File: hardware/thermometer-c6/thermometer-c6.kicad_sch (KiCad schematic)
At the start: 99 parts, among them J1 JST-PH-2 BAT, J2 MEAS_HDR, J3 USB-C, J4 EPD FPC24 0.5mm, J5 DEBUG, Q1 AO3401A, Q2 AO3401A, Q3 Si1308EDL, Q4 AO3401A, Q5 2N7002, Q6 AO3401A, SW1 RESET, SW2 BOOT, U1 ESP32-C6-MINI-1-N4, U2 RT9080-33GJ5, U3 USBLC6-2SC6, U4 MCP73831-2, U5 BMP581, U6 BMP585, Y1 32.768kHz FC-135

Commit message: Draw XUNPU FPC-05FB-24PH20 footprint, swap J4 off the Hirose stand-in
Land pattern transcribed from the XUNPU FPC-05FB-NPH20 manufacture
drawing and cross-checked against the EasyEDA/JLC C2856831 pattern
(exact match): 24 pads 0.3x1.2 @0.5mm, tabs 2.0x1.8 at +/-7.3/+1.625.
Cable enters from the pad-row side, actuator flips at the rear, pin 1
on the right with cable entry up (silk dot).

Co-Authored-By: Claude Fable 5 <noreply@anthropic.com>
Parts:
- J4: footprint Connector_FFC-FPC:Hirose_FH12-24S-0.5SH_1x24-1MP_P0.50mm_Horizontal -> local:XUNPU_FPC-05FB-24PH20
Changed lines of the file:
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@@
       )
     )
-    (property "Footprint" "Connector_FFC-FPC:Hirose_FH12-24S-0.5SH_1x24-1MP_P0.50mm_Horizontal"
+    (property "Footprint" "local:XUNPU_FPC-05FB-24PH20"
       (at 215.9 185.42 0)
       (effects

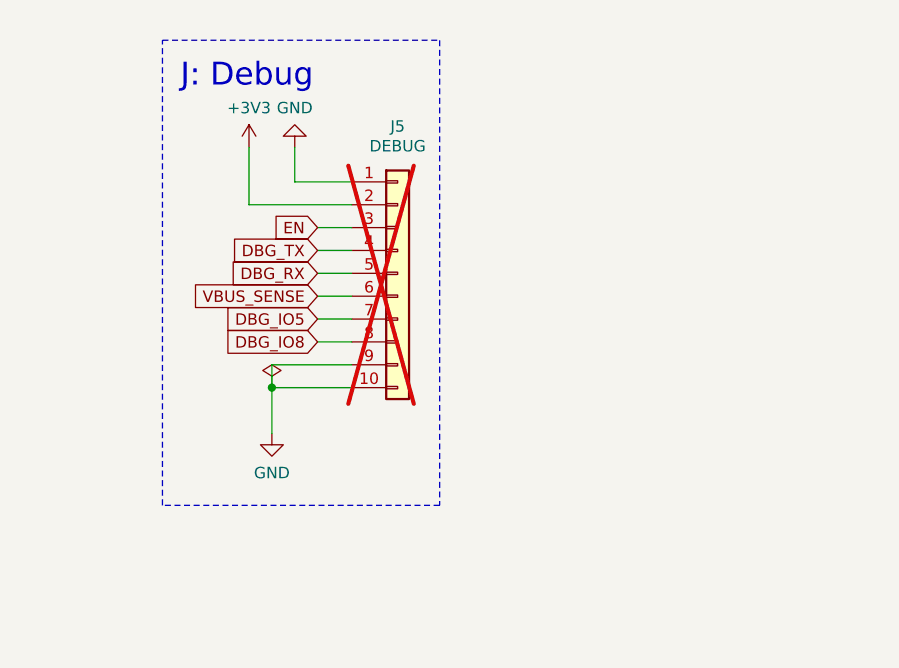
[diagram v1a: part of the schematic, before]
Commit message: Add scripted PCB generator: pcb.py renders the board from pcb_layout.py
generator/pcb.py builds thermometer-c6.kicad_pcb with the pcbnew API:
nets carry the kicad-cli-exported names (schematic parity green from the
start), footprints link their symbol UUIDs, and a text post-pass sorts
item blocks and rewrites UUIDs so regeneration is byte-stable. A
generated .kicad_dru enforces 0.3mm clearance on the +/-20V EPD nets
(zones included) and 0.5mm width on the battery-current paths.

ZONE_FILLER segfaults on a project-less CreateEmptyBoard board; the
generator saves, reloads with LoadBoard, fills, and saves again.

local:ESP32-C6-MINI-1 is the stock footprint with a body-sized courtyard
(the stock 43x32mm courtyard/rule-area is drawn for mid-board placement);
the board adds its own antenna keep-out at placement. H1/H2 M2 mounting
holes join circuit.py so the PCB has no board-only footprints, and
TPs/jumpers/holes are now in_bom=no on both sides. pcb_layout.py holds a
provisional parking grid until the placement pass.

Makefile: pcb / drc / pcb-img targets (drc not yet in the check gate --
routing pending).

Co-Authored-By: Claude Fable 5 <noreply@anthropic.com>
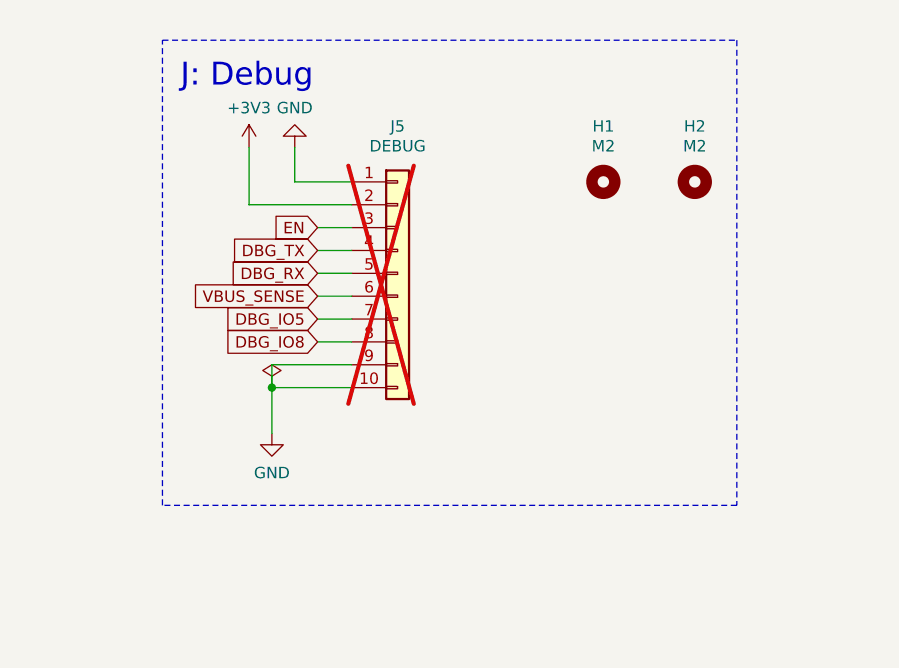
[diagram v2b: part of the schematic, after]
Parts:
- added H1, H2: M2, MountingHole:MountingHole_2.2mm_M2, symbol Mechanical:MountingHole
- JP1, JP2, JP3, JP4, JP5, JP6, TP1, TP10, TP11, TP2, TP3, TP4, TP5, TP6, TP7, TP8, TP9: now left out of the parts list
- U1: footprint RF_Module:ESP32-C6-MINI-1 -> local:ESP32-C6-MINI-1
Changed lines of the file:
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@@
     (unit 1)
     (exclude_from_sim no)
-    (in_bom yes)
+    (in_bom no)
     (on_board yes)
     (dnp no)
@@
     (unit 1)
     (exclude_from_sim no)
-    (in_bom yes)
+    (in_bom no)
     (on_board yes)
     (dnp no)
@@
     (unit 1)
     (exclude_from_sim no)
-    (in_bom yes)
+    (in_bom no)
     (on_board yes)
     (dnp no)
@@
     (unit 1)
     (exclude_from_sim no)
-    (in_bom yes)
+    (in_bom no)
     (on_board yes)
     (dnp no)
@@
     (unit 1)
     (exclude_from_sim no)
-    (in_bom yes)
+    (in_bom no)
     (on_board yes)
     (dnp no)
@@
       )
     )
-    (property "Footprint" "RF_Module:ESP32-C6-MINI-1"
+    (property "Footprint" "local:ESP32-C6-MINI-1"
       (at 355.6 60.96 0)
       (effects
@@
     (unit 1)
     (exclude_from_sim no)
-    (in_bom yes)
+    (in_bom no)
     (on_board yes)
     (dnp no)
@@
     (unit 1)
     (exclude_from_sim no)
-    (in_bom yes)
+    (in_bom no)
     (on_board yes)
     (dnp no)
@@
     (unit 1)
     (exclude_from_sim no)
-    (in_bom yes)
+    (in_bom no)
     (on_board yes)
     (dnp no)
@@
     (unit 1)
     (exclude_from_sim no)
-    (in_bom yes)
+    (in_bom no)
     (on_board yes)
     (dnp no)
@@
     (unit 1)
     (exclude_from_sim no)
-    (in_bom yes)
+    (in_bom no)
     (on_board yes)
     (dnp no)
@@
     (unit 1)
     (exclude_from_sim no)
-    (in_bom yes)
+    (in_bom no)
     (on_board yes)
     (dnp no)
@@
     (unit 1)
     (exclude_from_sim no)
-    (in_bom yes)
+    (in_bom no)
     (on_board yes)
     (dnp no)
@@
     (unit 1)
     (exclude_from_sim no)
-    (in_bom yes)
+    (in_bom no)
     (on_board yes)
     (dnp no)
@@
     (unit 1)
     (exclude_from_sim no)
-    (in_bom yes)
+    (in_bom no)
     (on_board yes)
     (dnp no)
@@
     (unit 1)
     (exclude_from_sim no)
-    (in_bom yes)
+    (in_bom no)
     (on_board yes)
     (dnp no)
@@
     (unit 1)
     (exclude_from_sim no)
-    (in_bom yes)
+    (in_bom no)
     (on_board yes)
     (dnp no)
@@
     (unit 1)
     (exclude_from_sim no)
-    (in_bom yes)
+    (in_bom no)
     (on_board yes)
     (dnp no)
@@
     )
   )
+  (symbol
+    (lib_id "Mechanical:MountingHole")
+    (at 534.67 30.48 0)
+    (unit 1)
+    (exclude_from_sim no)
+    (in_bom no)
+    (on_board yes)
+    (dnp no)
+    (property "Reference" "H1"
+      (at 534.67 24.31 0)
+      (effects
+        (font
+          (size 1.27 1.27)
+        )
+      )
+    )
+    (property "Value" "M2"
+      (at 534.67 26.51 0)
+      (effects
+        (font
+          (size 1.27 1.27)
+        )
+      )
+    )
+    (property "Footprint" "MountingHole:MountingHole_2.2mm_M2"
+      (at 534.67 30.48 0)
+      (effects
+        (font
+          (size 1.27 1.27)
+        )
+        (hide yes)
+      )
+    )
+    (property "Datasheet" "~"
+      (at 534.67 30.48 0)
+      (effects
+        (font
+          (size 1.27 1.27)
+        )
+        (hide yes)
+      )
+    )
+    (property "LCSC" ""
+      (at 534.67 30.48 0)
+      (effects
+        (font
+          (size 1.27 1.27)
+        )
+        (hide yes)
+      )
+    )
+    (instances
+      (project "thermometer-c6"
+        (path "/0f155dae-a0e5-543a-be87-8caf78dad21b"
+          (reference "H1")
+          (unit 1)
+        )
+      )
+    )
+  )
+  (symbol
+    (lib_id "Mechanical:MountingHole")
+    (at 544.83 30.48 0)
+    (unit 1)
+    (exclude_from_sim no)
+    (in_bom no)
+    (on_board yes)
+    (dnp no)
+    (property "Reference" "H2"
+      (at 544.83 24.31 0)
+      (effects
+        (font
+          (size 1.27 1.27)
+        )
+      )
+    )
+    (property "Value" "M2"
+      (at 544.83 26.51 0)
+      (effects
+        (font
+          (size 1.27 1.27)
+        )
+      )
+    )
+    (property "Footprint" "MountingHole:MountingHole_2.2mm_M2"
+      (at 544.83 30.48 0)
+      (effects
+        (font
+          (size 1.27 1.27)
+        )
+        (hide yes)
+      )
+    )
+    (property "Datasheet" "~"
+      (at 544.83 30.48 0)
+      (effects
+        (font
+          (size 1.27 1.27)
+        )
+        (hide yes)
+      )
+    )
+    (property "LCSC" ""
+      (at 544.83 30.48 0)
+      (effects
+        (font
+          (size 1.27 1.27)
+        )
+        (hide yes)
+      )
+    )
+    (instances
+      (project "thermometer-c6"
+        (path "/0f155dae-a0e5-543a-be87-8caf78dad21b"
+          (reference "H2")
+          (unit 1)
+        )
+      )
+    )
+  )
   (text "A: Battery + PPK2 break"
     (exclude_from_sim no)
@@
   (rectangle
     (start 485.68 14.74)
-    (end 516.48 66.42)
+    (end 549.5 66.42)
     (stroke
       (width 0.1)

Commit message: WIP power routing: battery chain, VBAT/VSYS/VBUS first pass
J5 debug header becomes a 2x5 (12.7mm vs 25.4mm inline). Sensor rule
areas now permit tracks (LGA escape routing is unavoidable; vias and
pour stay banned) and check_pcb distinguishes the strict antenna area
from the sensor areas. First batch of power tracks + vias authored in
pcb_layout.py: JST->Q6->JP1->J2 battery chain, VBAT rails, VSYS via a
north/west B.Cu lane, VBUS tree, CHG-LED feed.

KNOWN BAD: ~30 DRC violations cluster in the NE charger quadrant
(D2/U4/C6/Q1 lane congestion) and around the JP1 pocket - a derived
v2 rework exists in the session notes and still needs applying. DRC
is not yet in the check gate; make check stays green.

Co-Authored-By: Claude Fable 5 <noreply@anthropic.com>
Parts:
- J5: footprint Connector_PinHeader_2.54mm:PinHeader_1x10_P2.54mm_Vertical -> Connector_PinHeader_2.54mm:PinHeader_2x05_P2.54mm_Vertical
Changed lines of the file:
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@@
       )
     )
-    (property "Footprint" "Connector_PinHeader_2.54mm:PinHeader_1x10_P2.54mm_Vertical"
+    (property "Footprint" "Connector_PinHeader_2.54mm:PinHeader_2x05_P2.54mm_Vertical"
       (at 511.81 40.64 0)
       (effects

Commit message: Promote C29 to populated front-side part; M7 silk polish batch
C29 (10nF ADC reservoir): back DNP -> front populated at (12.6,27.7), dnp=False + LCSC C15195, routed (harvested from GUI). Netlist/pin-set unchanged; invariants desc, README, EE-PRIMER, BOM regenerated. Silk batch: 47uH value by JP6 (user spot 27.8,20.0); FPC pin 1/24 markers on J4; 'fit ONE'->'U5/U6 fit ONE'; bridge legend split to 3 spaced lines; 'CHARGE INDOORS 0-45C' contiguous; R9 10M label cleared of VBAT_ADC; TP4->'3V3 probe-only'; '3.7V LiPo' by J1 (on back - no front room); board name -> 'Low-Power E-Paper Thermometer  rev A'; looser back-silk line spacing; corrected C9/C14/C15 floorplan comment. Gate: 0 unconnected, 0 DRC (silk incl text-size all 0), check_pcb OK, make check green, byte-stable.

Co-Authored-By: Claude Opus 4.8 (1M context) <noreply@anthropic.com>
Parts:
- C29: LCSC (none) -> C15195; now fitted; now in the parts list
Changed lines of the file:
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@@
     (unit 1)
     (exclude_from_sim no)
-    (in_bom no)
+    (in_bom yes)
     (on_board yes)
-    (dnp yes)
+    (dnp no)
     (property "Reference" "C29"
       (at 398.44 184.22 0)
@@
       )
     )
-    (property "LCSC" ""
+    (property "LCSC" "C15195"
       (at 396.24 185.42 0)
       (effects

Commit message: Upgrade 4.7uF caps to 50V and make D7 TVS symbol unidirectional
Review follow-ups from REVIEW-KICAD-HAPPY.md: the booster/panel rails run
4.7uF/25V at up to +-22V DC bias (C17 PREVGH at 88% of rating); Samsung
CL21A475KBQNNNE (C98192, 50V X5R 0805) is a drop-in for all nine 4.7uF
refs, collapsing them into one BOM line with real derating margin. D7
(SMF5.0A, unidirectional) moves from the bidirectional D_TVS symbol to
D_Zener so schematic polarity is explicit for the hand-solder provision;
pin/net mapping unchanged (K=pin1=VBUS). Also refresh stale README notes:
BMP581 restocked (U5 populated by default) and Q6 reverse-battery
protection is fitted, not omitted.

Co-Authored-By: Claude Fable 5 <noreply@anthropic.com>
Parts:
- C16, C17, C18, C19, C20, C23, C24, C5, C6: value 4.7uF/25V -> 4.7uF/50V; LCSC C1779 -> C98192
- D7: symbol Device:D_TVS -> Device:D_Zener
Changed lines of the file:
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@@
       )
     )
-    (property "Value" "4.7uF/25V"
+    (property "Value" "4.7uF/50V"
       (at 287.36 41.476 0)
       (effects
@@
       )
     )
-    (property "LCSC" "C1779"
+    (property "LCSC" "C98192"
       (at 289.56 35.56 0)
       (effects
@@
       )
     )
-    (property "Value" "4.7uF/25V"
+    (property "Value" "4.7uF/50V"
       (at 265.09 82.48 0)
       (effects
@@
       )
     )
-    (property "LCSC" "C1779"
+    (property "LCSC" "C98192"
       (at 262.89 81.28 0)
       (effects
@@
   )
   (symbol
-    (lib_id "Device:D_TVS")
+    (lib_id "Device:D_Zener")
     (at 295.91 35.56 270)
     (unit 1)
@@
       )
     )
-    (property "Value" "4.7uF/25V"
+    (property "Value" "4.7uF/50V"
       (at 70.78 170.11 0)
       (effects
@@
       )
     )
-    (property "LCSC" "C1779"
+    (property "LCSC" "C98192"
       (at 68.58 168.91 0)
       (effects
@@
       )
     )
-    (property "Value" "4.7uF/25V"
+    (property "Value" "4.7uF/50V"
       (at 86.36 164.626 0)
       (effects
@@
       )
     )
-    (property "LCSC" "C1779"
+    (property "LCSC" "C98192"
       (at 86.36 156.21 0)
       (effects
@@
       )
     )
-    (property "Value" "4.7uF/25V"
+    (property "Value" "4.7uF/50V"
       (at 97.45 177.73 0)
       (effects
@@
       )
     )
-    (property "LCSC" "C1779"
+    (property "LCSC" "C98192"
       (at 95.25 176.53 0)
       (effects
@@
       )
     )
-    (property "Value" "4.7uF/25V"
+    (property "Value" "4.7uF/50V"
       (at 201.93 172.5 90)
       (effects
@@
       )
     )
-    (property "LCSC" "C1779"
+    (property "LCSC" "C98192"
       (at 201.93 165.1 0)
       (effects
@@
       )
     )
-    (property "Value" "4.7uF/25V"
+    (property "Value" "4.7uF/50V"
       (at 189.23 172.54 90)
       (effects
@@
       )
     )
-    (property "LCSC" "C1779"
+    (property "LCSC" "C98192"
       (at 189.23 167.64 0)
       (effects
@@
       )
     )
-    (property "Value" "4.7uF/25V"
+    (property "Value" "4.7uF/50V"
       (at 186.014 210.64 90)
       (effects
@@
       )
     )
-    (property "LCSC" "C1779"
+    (property "LCSC" "C98192"
       (at 189.23 205.74 0)
       (effects
@@
       )
     )
-    (property "Value" "4.7uF/25V"
+    (property "Value" "4.7uF/50V"
       (at 190.5 229.396 0)
       (effects
@@
       )
     )
-    (property "LCSC" "C1779"
+    (property "LCSC" "C98192"
       (at 190.5 220.98 0)
       (effects

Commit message: Swap D3 status LED to basic white C2290, correct ordering doc
JLC's basic list has no green 0603 LED (green is 0805-only), so the
STATUS LED becomes white to drop one Extended feeder fee. ORDERING.md:
Economy PCBA is impossible (ENIG + POFV + U1/U5 Standard-only), and
"Remove Mark" must not be selected or the JLCJLCJLCJLC token prints
literally.

Co-Authored-By: Claude Fable 5 <noreply@anthropic.com>
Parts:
- D3: value STATUS green -> STATUS white; LCSC C12624 -> C2290
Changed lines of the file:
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@@
       )
     )
-    (property "Value" "STATUS green"
+    (property "Value" "STATUS white"
       (at 423.84 107.88 270)
       (effects
@@
       )
     )
-    (property "LCSC" "C12624"
+    (property "LCSC" "C2290"
       (at 421.64 106.68 0)
       (effects

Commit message: Re-place J3 on its true datum, fork its land, and drop the edge waiver
out/j3-datum/ parsed the HRO TYPE-C-31-M-12 datasheet's vector content stream
(plus a 1200dpi raster pass and the STEP, three methods agreeing to <=0.005mm)
and showed the placement datum was misread: "5.79" is measured PCB EDGE ->
NPTH plastic-post CENTRELINE, not to the SMT pad row, and "4.18" is shell-slot
centre to shell-slot centre. The front shell slot therefore belongs 2.11mm from
the north edge, not 0.695 -- J3 sat 1.415mm too far north.

PLACE["J3"] y 1.745 -> 3.160 (x and the 180 rotation unchanged). Front slots
land at 2.110 (datasheet 2.1078), rear at 6.290, NPTH at 5.760, pad row at
7.035; the mouth still overhangs 0.490mm as an edge-launch part should.

The land was wrong too (out/j3-land/): with the solder foot measured at 0.850mm
from the STEP -- isolated by gold colour + Z-normal planarity + z=0, not by
z-slicing a point cloud -- the stock KiCad land left only +0.080mm heel
protrusion, below IPC-7351B Least (0.25) and negative under the tolerance
stack, while spending +0.520 on toe. The footprint is now a project fork,
local:USB_C_Receptacle_HRO_TYPE-C-31-M-12, with the SMT row 0.170mm toward the
mouth and the NPTH posts 0.65 -> 0.60mm (HRO's own value; it is what makes the
shift legal at the 0.25mm hole_clearance rule, and it halves the dominant
registration tolerance). Heel is now +0.250, toe +0.350, and 100% of the
0.200mm heel-fillet zone is covered. Pad sizes, x, pitch, shape and names are
untouched. MODELS_3D re-keyed to the new fpid (it is keyed by fpid string, so a
missed re-key silently detaches the model), and the model offset re-solved to
the peg-exact oy=-1.050: front legs and both posts land at 0.000 residual, rear
legs at 0.005 (the model's 4.175mm leg span vs the land's 4.180 -- irreducible),
and the feet then sit inside the pad at exactly heel 0.250 / toe 0.350. The old
-0.94 was a compromise splitting 0.22mm between pegs and feet; that 0.22mm WAS
this land error.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
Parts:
- J3: footprint Connector_USB:USB_C_Receptacle_HRO_TYPE-C-31-M-12 -> local:USB_C_Receptacle_HRO_TYPE-C-31-M-12
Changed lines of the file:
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@@
       )
     )
-    (property "Footprint" "Connector_USB:USB_C_Receptacle_HRO_TYPE-C-31-M-12"
+    (property "Footprint" "local:USB_C_Receptacle_HRO_TYPE-C-31-M-12"
       (at 203.2 53.34 0)
       (effects
